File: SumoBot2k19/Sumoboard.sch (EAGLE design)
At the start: 37 parts

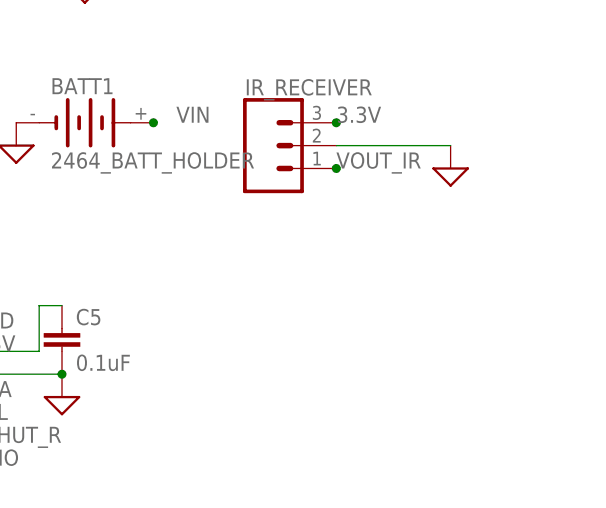
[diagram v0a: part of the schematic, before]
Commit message: changed the battery footprint
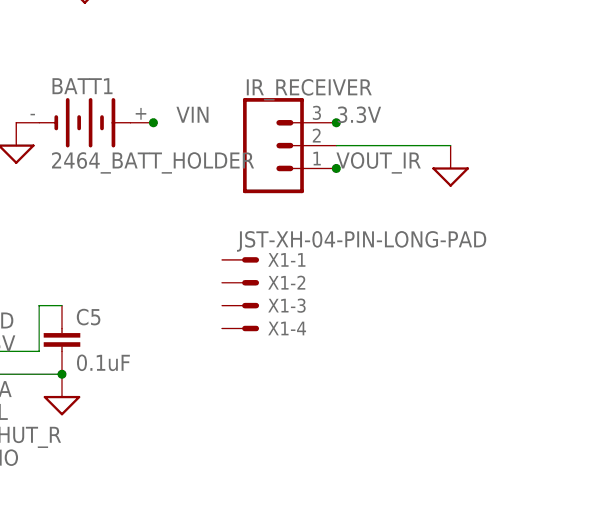
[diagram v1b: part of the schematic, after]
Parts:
- added X1: JST-XH-04-PIN-LONG-PAD, Rembrandt Electronics - JST XH Connectors v1-0:JST-XH-04-PIN-LONG-PAD
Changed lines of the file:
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@@
 <part name="GND19" library="audio amplifier example" library_urn="urn:adsk.eagle:library:970892" deviceset="GND" device="" value="SUP"/>
 <part name="GND26" library="audio amplifier example" library_urn="urn:adsk.eagle:library:970892" deviceset="GND" device="" value="SUP"/>
+<part name="X1" library="Rembrandt Electronics - JST XH Connectors v1-0" deviceset="JST-XH-04-PIN" device="-LONG-PAD"/>
 </parts>
 <sheets>
@@
 <instance part="GND19" gate="G$1" x="172.72" y="101.6" smashed="yes"/>
 <instance part="GND26" gate="G$1" x="172.72" y="83.82" smashed="yes"/>
+<instance part="X1" gate="-1" x="152.4" y="27.94" smashed="yes">
+<attribute name="NAME" x="154.94" y="27.178" size="1.524" layer="95"/>
+<attribute name="VALUE" x="151.638" y="29.337" size="1.778" layer="96"/>
+</instance>
+<instance part="X1" gate="-2" x="152.4" y="25.4" smashed="yes">
+<attribute name="NAME" x="154.94" y="24.638" size="1.524" layer="95"/>
+</instance>
+<instance part="X1" gate="-3" x="152.4" y="22.86" smashed="yes">
+<attribute name="NAME" x="154.94" y="22.098" size="1.524" layer="95"/>
+</instance>
+<instance part="X1" gate="-4" x="152.4" y="20.32" smashed="yes">
+<attribute name="NAME" x="154.94" y="19.558" size="1.524" layer="95"/>
+</instance>
 </instances>
 <busses>

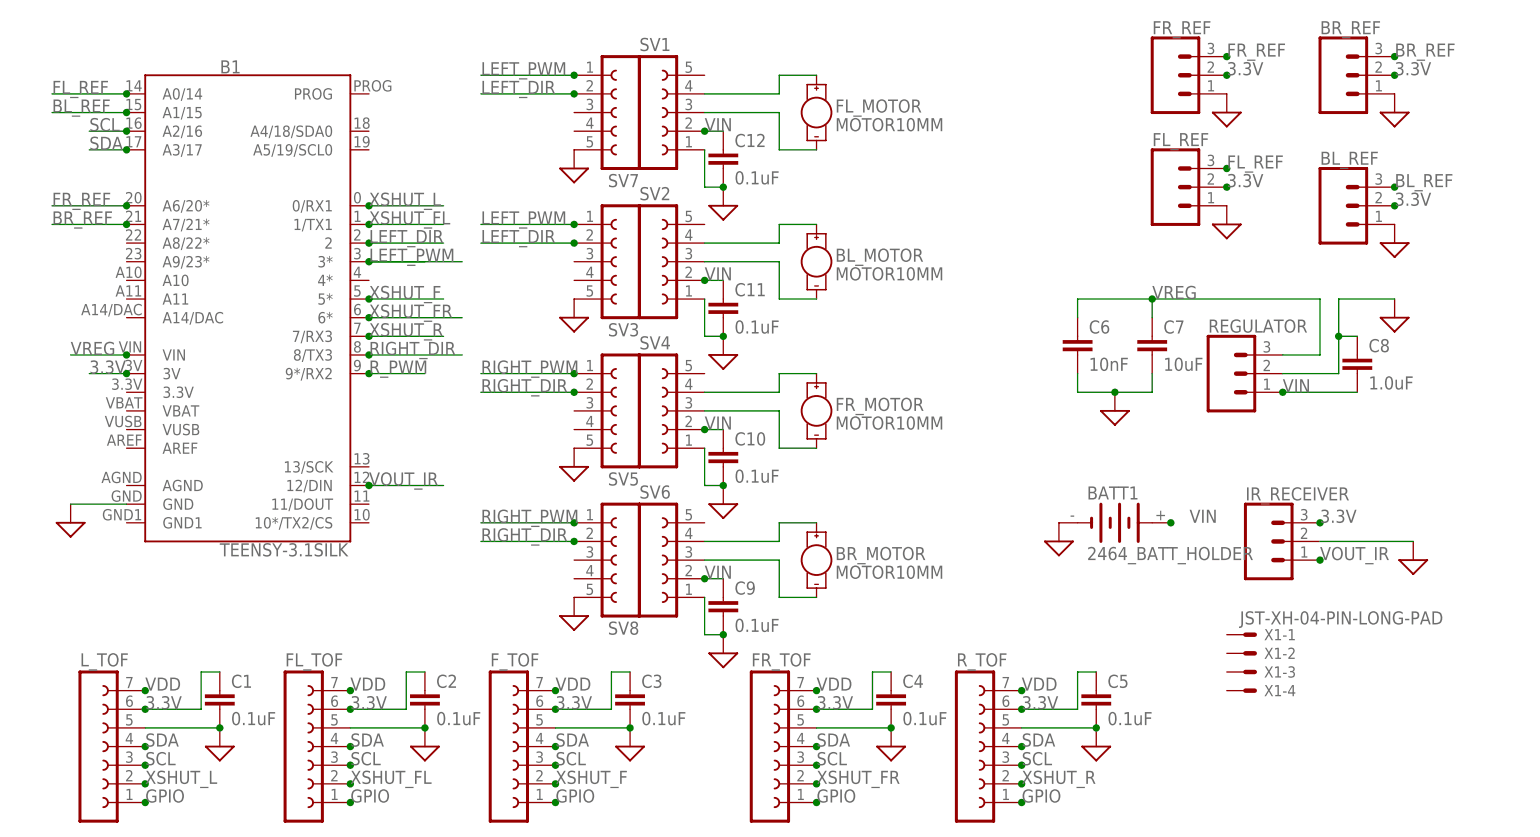
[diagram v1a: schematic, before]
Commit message: changed motors and battery to match desired JST-XH footprint on PCB
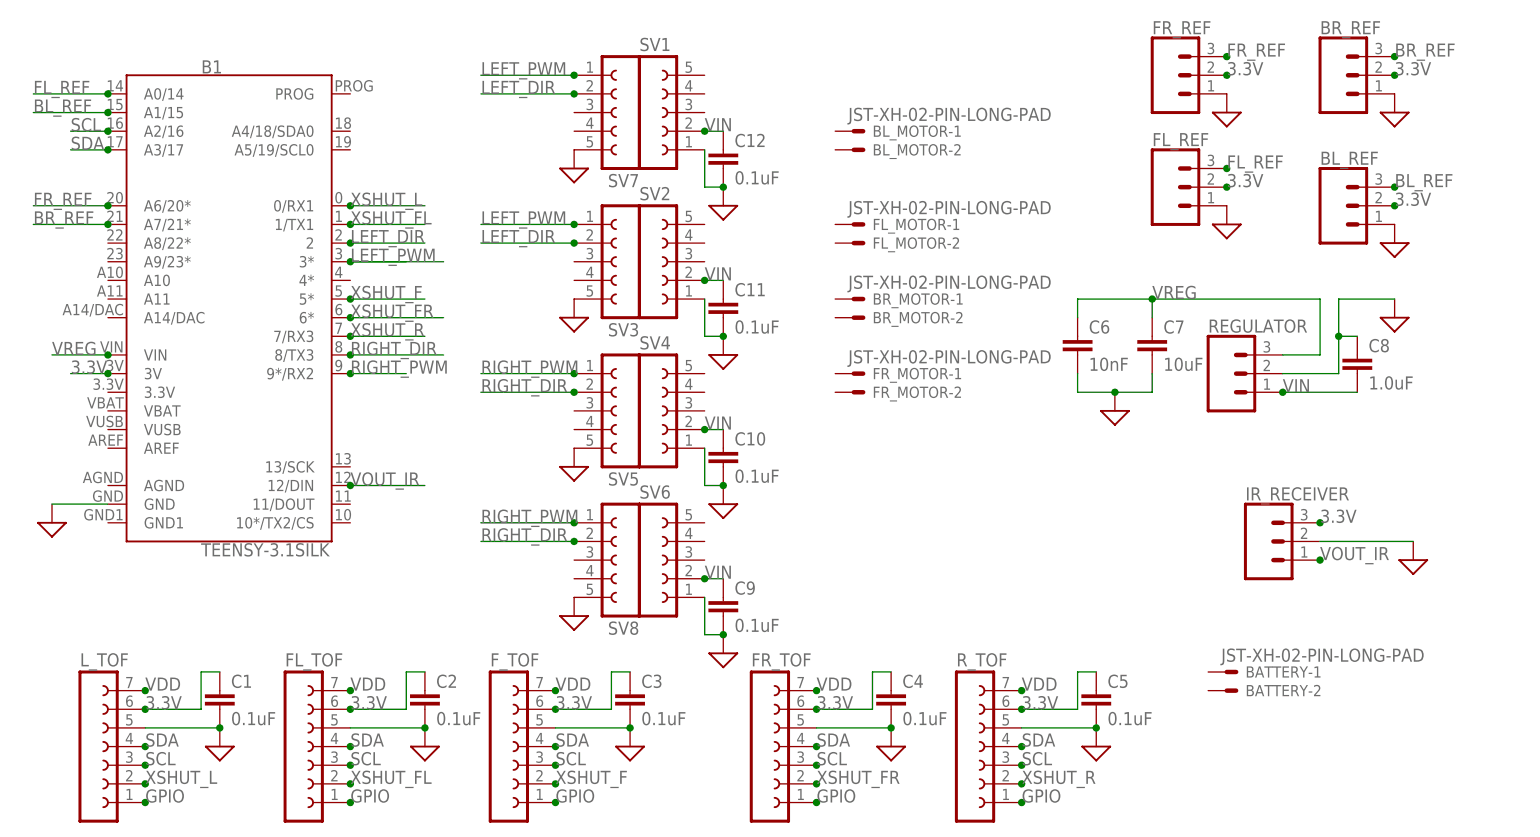
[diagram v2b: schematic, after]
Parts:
- removed BATT1: 2464_BATT_HOLDER, DC_LOAD_AU:2464_BATT_HOLDER
- removed X1: JST-XH-04-PIN-LONG-PAD, Rembrandt Electronics - JST XH Connectors v1-0:JST-XH-04-PIN-LONG-PAD
- added BATTERY: JST-XH-02-PIN-LONG-PAD, Rembrandt Electronics - JST XH Connectors v1-0:JST-XH-02-PIN-LONG-PAD
- BL_MOTOR, BR_MOTOR, FL_MOTOR, FR_MOTOR: value MOTOR10MM -> JST-XH-02-PIN-LONG-PAD; device SparkFun-Electromechanical:MOTOR10MM -> Rembrandt Electronics - JST XH Connectors v1-0:JST-XH-02-PIN-LONG-PAD
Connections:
- removed net N$1: FL_MOTOR.+, SV1.4
- removed net N$15: BL_MOTOR.+, SV2.4
- removed net N$16: BL_MOTOR.-, SV2.3
- removed net N$19: FR_MOTOR.+, SV4.4
- removed net N$2: FL_MOTOR.-, SV1.3
- removed net N$20: FR_MOTOR.-, SV4.3
- removed net N$23: BR_MOTOR.+, SV6.4
- removed net N$24: BR_MOTOR.-, SV6.3
- removed net R_PWM: B1.9*/RX2
- net GND: no longer BATT1.-
- net RIGHT_PWM: now also B1.9*/RX2
- net VIN: no longer BATT1.+
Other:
- moved on the sheet: B1

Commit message: added connnections lol
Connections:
- new net N$1: BL_MOTOR-2.S, SV1.3
- new net N$2: BL_MOTOR-1.S, SV1.4
- new net N$3: BR_MOTOR-1.S, SV4.4
- new net N$4: BR_MOTOR-2.S, SV4.3
- new net N$5: FL_MOTOR-1.S, SV2.4
- new net N$6: FL_MOTOR-2.S, SV2.3
- new net N$7: FR_MOTOR-1.S, SV6.4
- new net N$8: FR_MOTOR-2.S, SV6.3
- net GND: now also BATTERY-2.S
- net VIN: now also BATTERY-1.S
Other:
- moved on the sheet: BL_MOTOR-1, BL_MOTOR-2, BR_MOTOR-1, BR_MOTOR-2, FL_MOTOR-1, FL_MOTOR-2, FR_MOTOR-1, FR_MOTOR-2
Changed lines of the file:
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@@
 <part name="FR_MOTOR" library="Rembrandt Electronics - JST XH Connectors v1-0" deviceset="JST-XH-02-PIN" device="-LONG-PAD"/>
 <part name="BATTERY" library="Rembrandt Electronics - JST XH Connectors v1-0" deviceset="JST-XH-02-PIN" device="-LONG-PAD"/>
+<part name="GND1" library="audio amplifier example" library_urn="urn:adsk.eagle:library:970892" deviceset="GND" device="" value="SUP"/>
 </parts>
 <sheets>
@@
 <instance part="GND19" gate="G$1" x="172.72" y="101.6" smashed="yes"/>
 <instance part="GND26" gate="G$1" x="172.72" y="83.82" smashed="yes"/>
-<instance part="BL_MOTOR" gate="-2" x="99.06" y="93.98" smashed="yes">
-<attribute name="NAME" x="101.6" y="93.218" size="1.524" layer="95"/>
-</instance>
-<instance part="BL_MOTOR" gate="-1" x="99.06" y="96.52" smashed="yes">
-<attribute name="NAME" x="101.6" y="95.758" size="1.524" layer="95"/>
-<attribute name="VALUE" x="98.298" y="97.917" size="1.778" layer="96"/>
-</instance>
-<instance part="FL_MOTOR" gate="-2" x="99.06" y="81.28" smashed="yes">
-<attribute name="NAME" x="101.6" y="80.518" size="1.524" layer="95"/>
-</instance>
-<instance part="FL_MOTOR" gate="-1" x="99.06" y="83.82" smashed="yes">
-<attribute name="NAME" x="101.6" y="83.058" size="1.524" layer="95"/>
-<attribute name="VALUE" x="98.298" y="85.217" size="1.778" layer="96"/>
-</instance>
-<instance part="BR_MOTOR" gate="-2" x="99.06" y="71.12" smashed="yes">
-<attribute name="NAME" x="101.6" y="70.358" size="1.524" layer="95"/>
-</instance>
-<instance part="BR_MOTOR" gate="-1" x="99.06" y="73.66" smashed="yes">
-<attribute name="NAME" x="101.6" y="72.898" size="1.524" layer="95"/>
-<attribute name="VALUE" x="98.298" y="75.057" size="1.778" layer="96"/>
-</instance>
-<instance part="FR_MOTOR" gate="-2" x="99.06" y="60.96" smashed="yes">
-<attribute name="NAME" x="101.6" y="60.198" size="1.524" layer="95"/>
-</instance>
-<instance part="FR_MOTOR" gate="-1" x="99.06" y="63.5" smashed="yes">
-<attribute name="NAME" x="101.6" y="62.738" size="1.524" layer="95"/>
-<attribute name="VALUE" x="98.298" y="64.897" size="1.778" layer="96"/>
+<instance part="BL_MOTOR" gate="-2" x="88.9" y="99.06" smashed="yes">
+<attribute name="NAME" x="91.44" y="98.298" size="1.524" layer="95"/>
+</instance>
+<instance part="BL_MOTOR" gate="-1" x="88.9" y="101.6" smashed="yes">
+<attribute name="NAME" x="91.44" y="100.838" size="1.524" layer="95"/>
+<attribute name="VALUE" x="88.138" y="102.997" size="1.778" layer="96"/>
+</instance>
+<instance part="FL_MOTOR" gate="-2" x="88.9" y="78.74" smashed="yes">
+<attribute name="NAME" x="91.44" y="77.978" size="1.524" layer="95"/>
+</instance>
+<instance part="FL_MOTOR" gate="-1" x="88.9" y="81.28" smashed="yes">
+<attribute name="NAME" x="91.44" y="80.518" size="1.524" layer="95"/>
+<attribute name="VALUE" x="88.138" y="82.677" size="1.778" layer="96"/>
+</instance>
+<instance part="BR_MOTOR" gate="-2" x="88.9" y="58.42" smashed="yes">
+<attribute name="NAME" x="91.44" y="57.658" size="1.524" layer="95"/>
+</instance>
+<instance part="BR_MOTOR" gate="-1" x="88.9" y="60.96" smashed="yes">
+<attribute name="NAME" x="91.44" y="60.198" size="1.524" layer="95"/>
+<attribute name="VALUE" x="88.138" y="62.357" size="1.778" layer="96"/>
+</instance>
+<instance part="FR_MOTOR" gate="-2" x="88.9" y="38.1" smashed="yes">
+<attribute name="NAME" x="91.44" y="37.338" size="1.524" layer="95"/>
+</instance>
+<instance part="FR_MOTOR" gate="-1" x="88.9" y="40.64" smashed="yes">
+<attribute name="NAME" x="91.44" y="39.878" size="1.524" layer="95"/>
+<attribute name="VALUE" x="88.138" y="42.037" size="1.778" layer="96"/>
 </instance>
 <instance part="BATTERY" gate="-2" x="149.86" y="20.32" smashed="yes">
@@
 <attribute name="VALUE" x="149.098" y="24.257" size="1.778" layer="96"/>
 </instance>
+<instance part="GND1" gate="G$1" x="147.32" y="20.32" smashed="yes"/>
 </instances>
 <busses>
@@
 <pinref part="C8" gate="G$1" pin="2"/>
 <wire x1="157.48" y1="60.96" x2="167.64" y2="60.96" width="0.1524" layer="91"/>
+</segment>
+<segment>
+<pinref part="BATTERY" gate="-1" pin="S"/>
+<junction x="147.32" y="22.86"/>
+<label x="142.24" y="22.86" size="1.778" layer="95"/>
 </segment>
 </net>
@@
 <pinref part="BL_REF" gate="J$1" pin="1"/>
 <pinref part="GND26" gate="G$1" pin="GND"/>
+</segment>
+<segment>
+<pinref part="BATTERY" gate="-2" pin="S"/>
+<pinref part="GND1" gate="G$1" pin="GND"/>
 </segment>
 </net>
@@
 </segment>
 </net>
+<net name="N$1" class="0">
+<segment>
+<pinref part="SV1" gate="G$1" pin="3"/>
+<wire x1="78.74" y1="99.06" x2="86.36" y2="99.06" width="0.1524" layer="91"/>
+<pinref part="BL_MOTOR" gate="-2" pin="S"/>
+</segment>
+</net>
+<net name="N$2" class="0">
+<segment>
+<pinref part="SV1" gate="G$1" pin="4"/>
+<wire x1="78.74" y1="101.6" x2="86.36" y2="101.6" width="0.1524" layer="91"/>
+<pinref part="BL_MOTOR" gate="-1" pin="S"/>
+</segment>
+</net>
+<net name="N$3" class="0">
+<segment>
+<pinref part="SV4" gate="G$1" pin="4"/>
+<pinref part="BR_MOTOR" gate="-1" pin="S"/>
+<wire x1="78.74" y1="60.96" x2="86.36" y2="60.96" width="0.1524" layer="91"/>
+</segment>
+</net>
+<net name="N$4" class="0">
+<segment>
+<pinref part="BR_MOTOR" gate="-2" pin="S"/>
+<pinref part="SV4" gate="G$1" pin="3"/>
+<wire x1="86.36" y1="58.42" x2="78.74" y2="58.42" width="0.1524" layer="91"/>
+</segment>
+</net>
+<net name="N$5" class="0">
+<segment>
+<pinref part="SV2" gate="G$1" pin="4"/>
+<pinref part="FL_MOTOR" gate="-1" pin="S"/>
+<wire x1="78.74" y1="81.28" x2="86.36" y2="81.28" width="0.1524" layer="91"/>
+</segment>
+</net>
+<net name="N$6" class="0">
+<segment>
+<pinref part="FL_MOTOR" gate="-2" pin="S"/>
+<pinref part="SV2" gate="G$1" pin="3"/>
+<wire x1="86.36" y1="78.74" x2="78.74" y2="78.74" width="0.1524" layer="91"/>
+</segment>
+</net>
+<net name="N$7" class="0">
+<segment>
+<pinref part="SV6" gate="G$1" pin="4"/>
+<pinref part="FR_MOTOR" gate="-1" pin="S"/>
+<wire x1="78.74" y1="40.64" x2="86.36" y2="40.64" width="0.1524" layer="91"/>
+</segment>
+</net>
+<net name="N$8" class="0">
+<segment>
+<pinref part="SV6" gate="G$1" pin="3"/>
+<pinref part="FR_MOTOR" gate="-2" pin="S"/>
+<wire x1="78.74" y1="38.1" x2="86.36" y2="38.1" width="0.1524" layer="91"/>
+</segment>
+</net>
